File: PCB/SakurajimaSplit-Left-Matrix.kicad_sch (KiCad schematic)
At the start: 42 parts, among them SW1 ESC, SW10 D, SW11 F, SW12 G, SW13 SW_Push_45deg, SW14 Z, SW15 X, SW16 C, SW17 V, SW18 B, SW19 SW_Push_45deg, SW2 Q, SW20 SW_Push_45deg, SW21 SW_Push_45deg, SW3 W, SW4 E, SW5 R, SW6 T, SW7 SW_Push_45deg, SW8 A, SW9 S

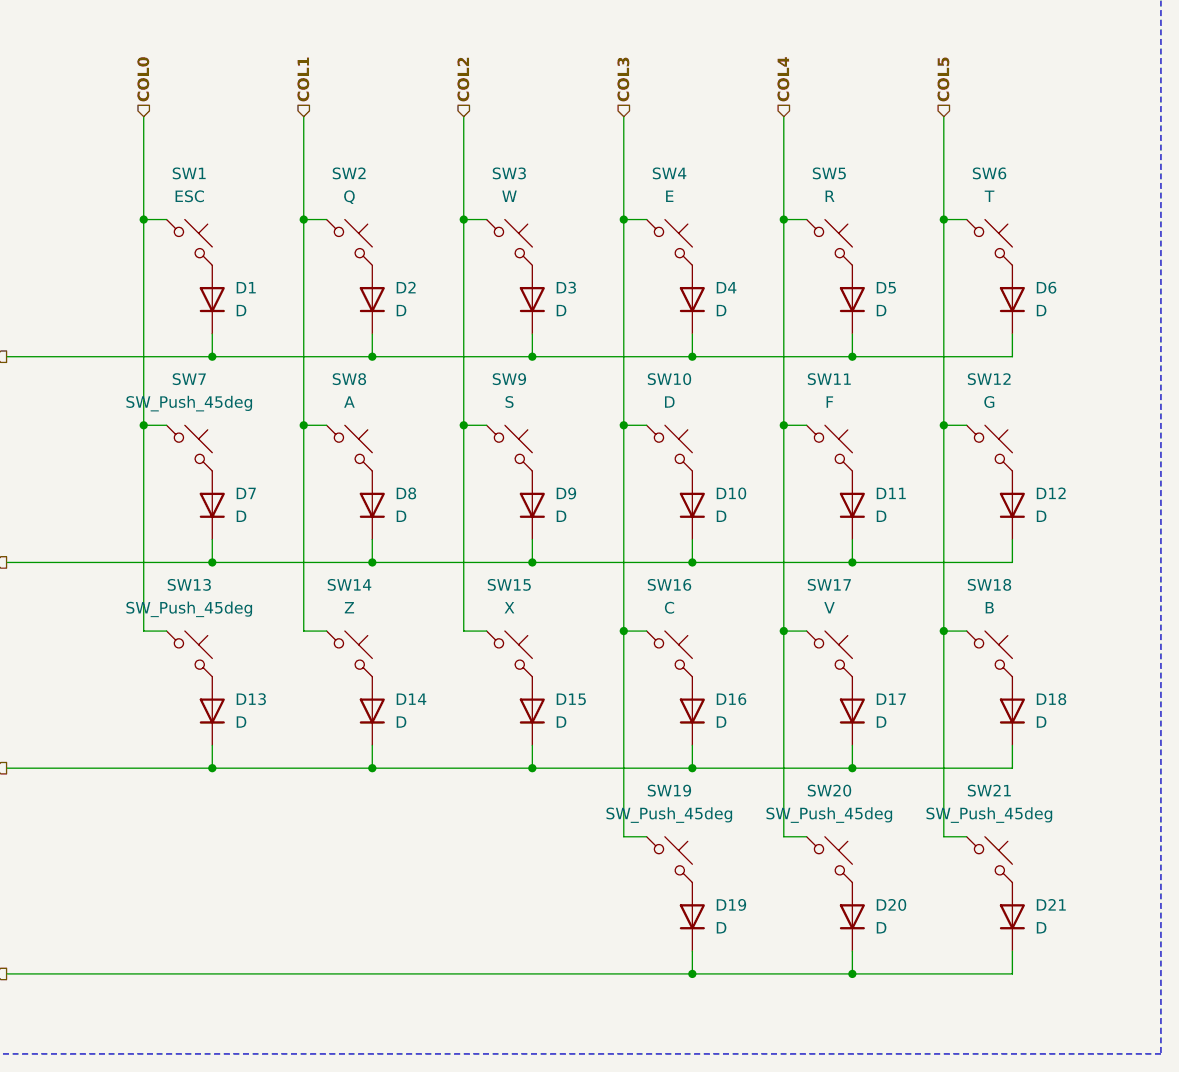
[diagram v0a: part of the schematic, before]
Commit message: feat(sch): add host USB connection and power circuit
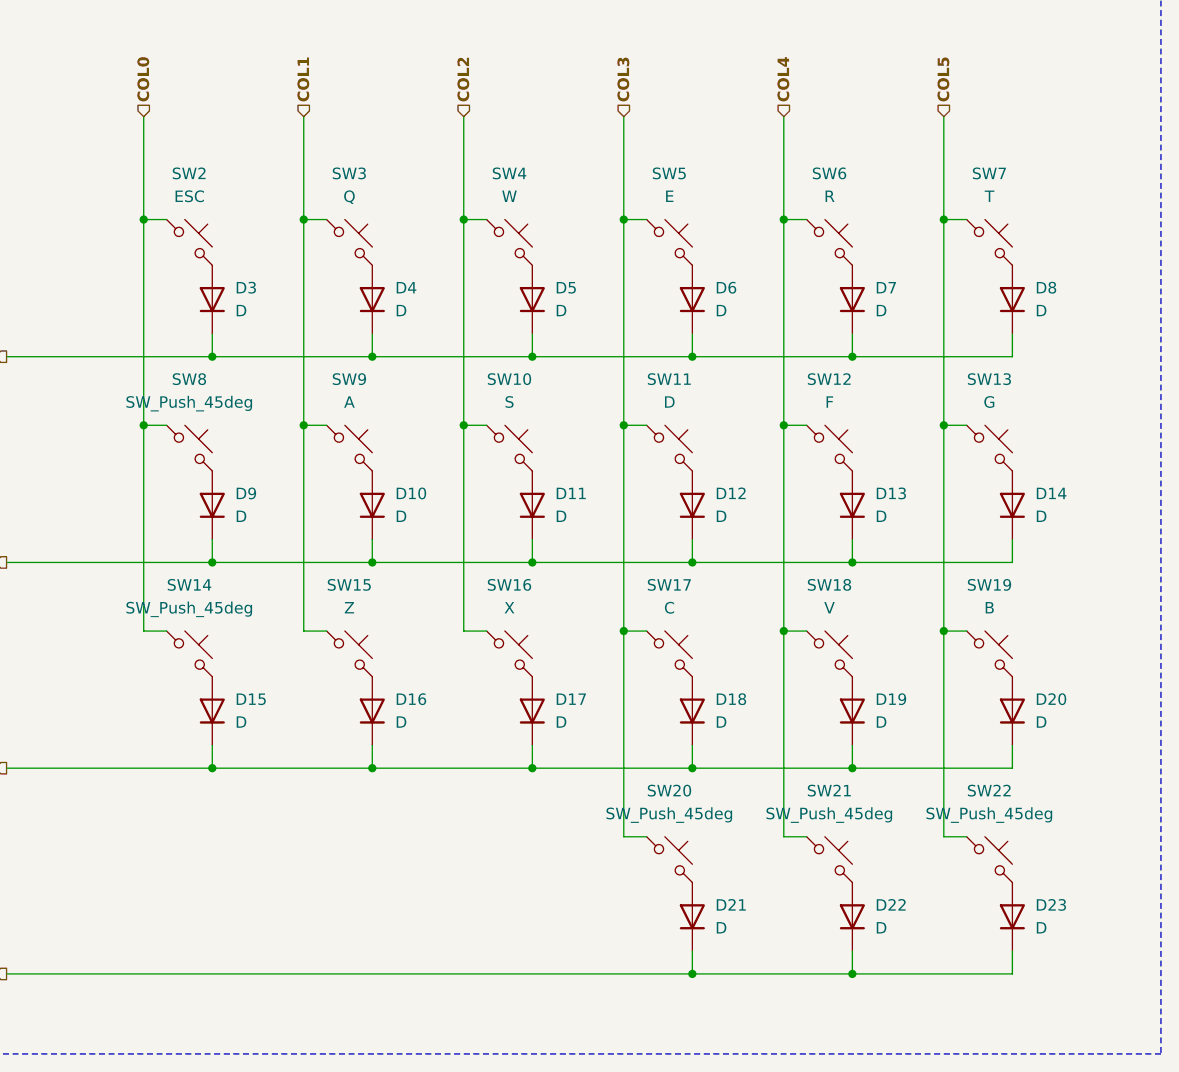
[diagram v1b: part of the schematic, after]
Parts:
- renumbered D8 to D10, D9 to D11, D10 to D12, D11 to D13, D12 to D14, D13 to D15, D14 to D16, D15 to D17, D16 to D18, D17 to D19, D18 to D20, D19 to D21, D20 to D22, D21 to D23, D1 to D3, D2 to D4, D3 to D5, D4 to D6, D5 to D7, D6 to D8, D7 to D9, SW9 to SW10, SW10 to SW11, SW11 to SW12, SW12 to SW13, SW13 to SW14, SW14 to SW15, SW15 to SW16, SW16 to SW17, SW17 to SW18, SW18 to SW19, SW1 to SW2, SW19 to SW20, SW20 to SW21, SW21 to SW22, SW2 to SW3, SW3 to SW4, SW4 to SW5, SW5 to SW6, SW6 to SW7, SW7 to SW8, SW8 to SW9

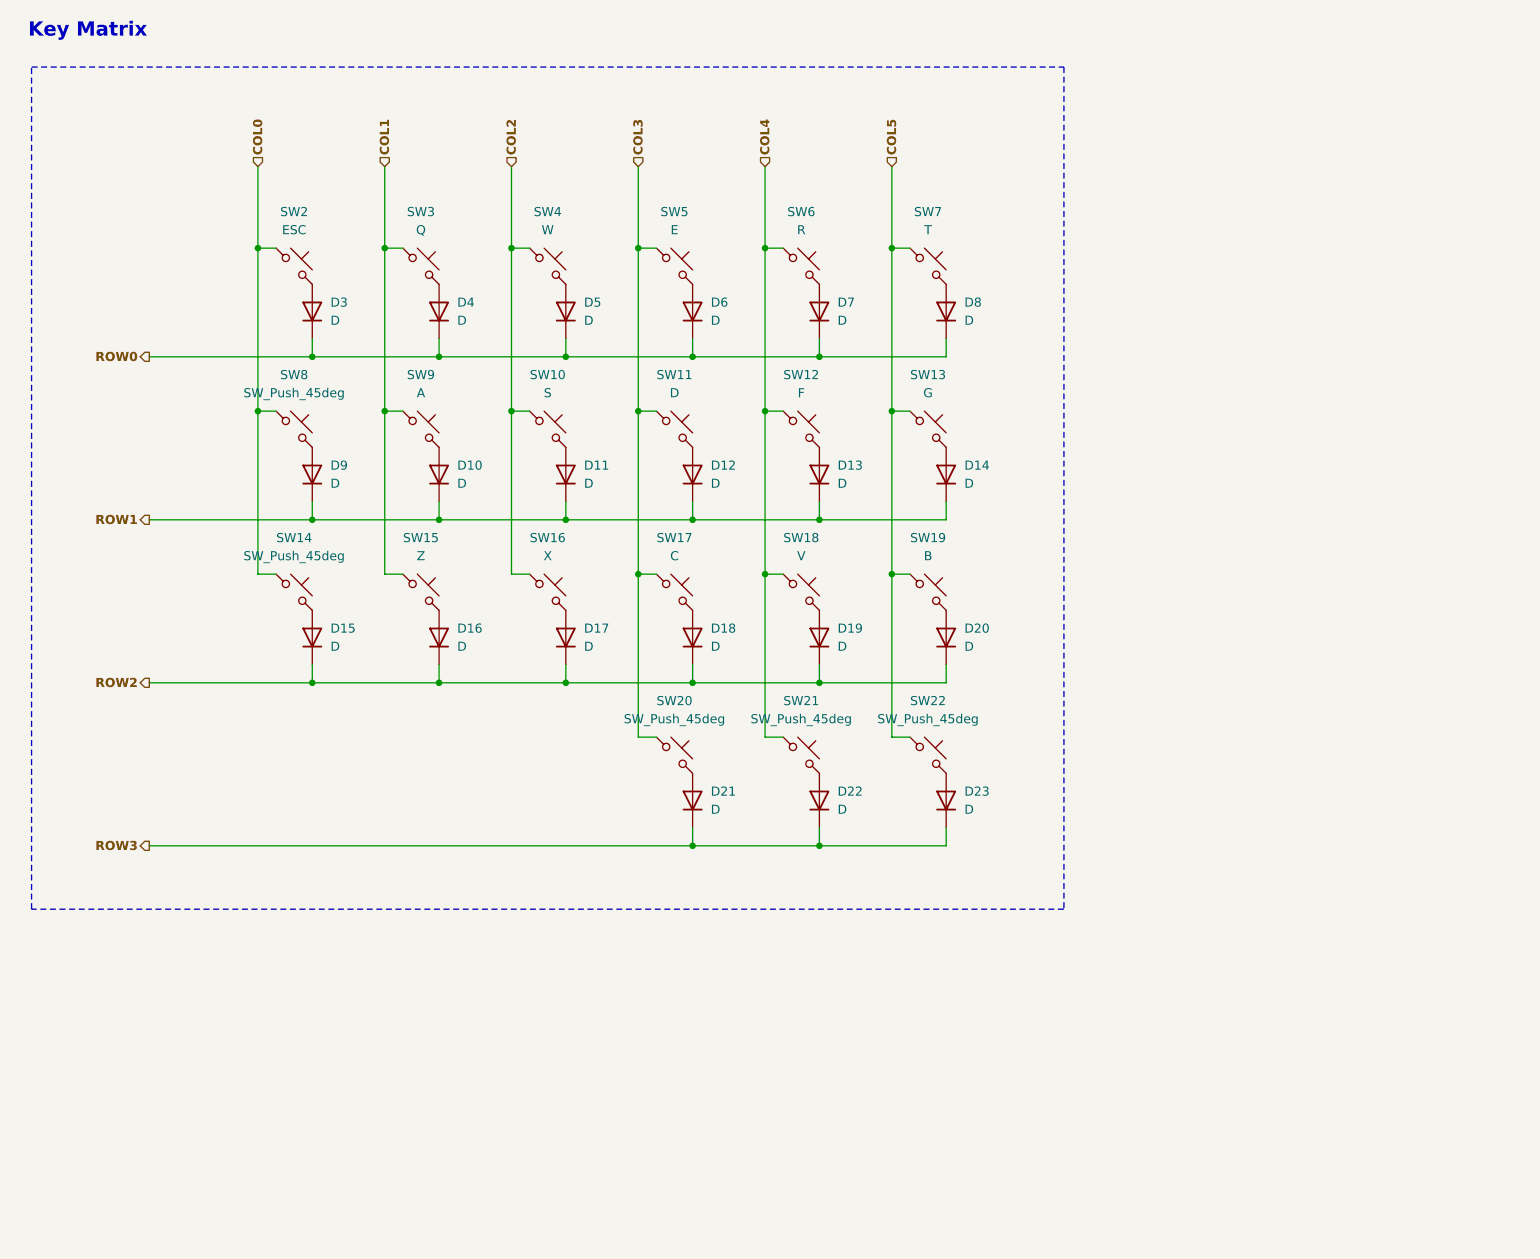
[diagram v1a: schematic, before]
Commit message: feat(sch): add USB to right-half circuit
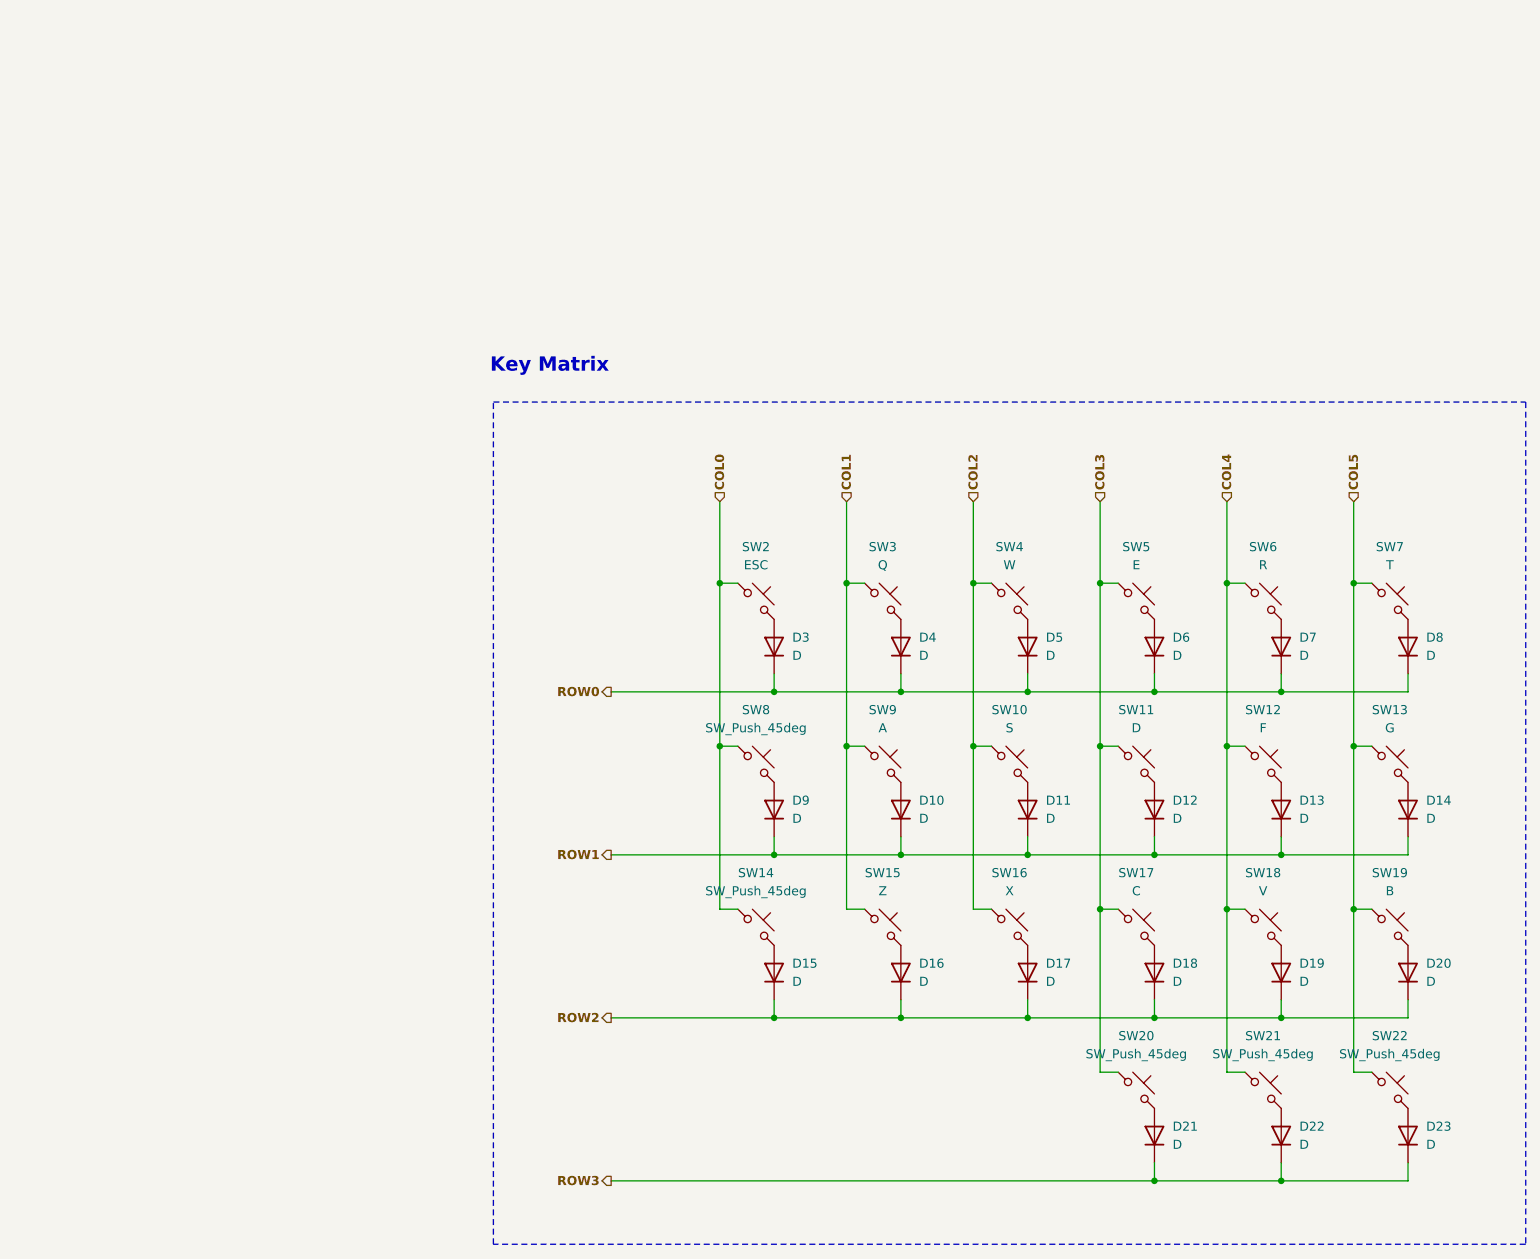
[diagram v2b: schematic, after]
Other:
- moved on the sheet: D10, D11, D12, D13, D14, D15, D16, D17, D18, D19, D20, D21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
